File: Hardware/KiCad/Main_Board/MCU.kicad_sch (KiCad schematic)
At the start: 1 part, among them U2 Teensy4.1

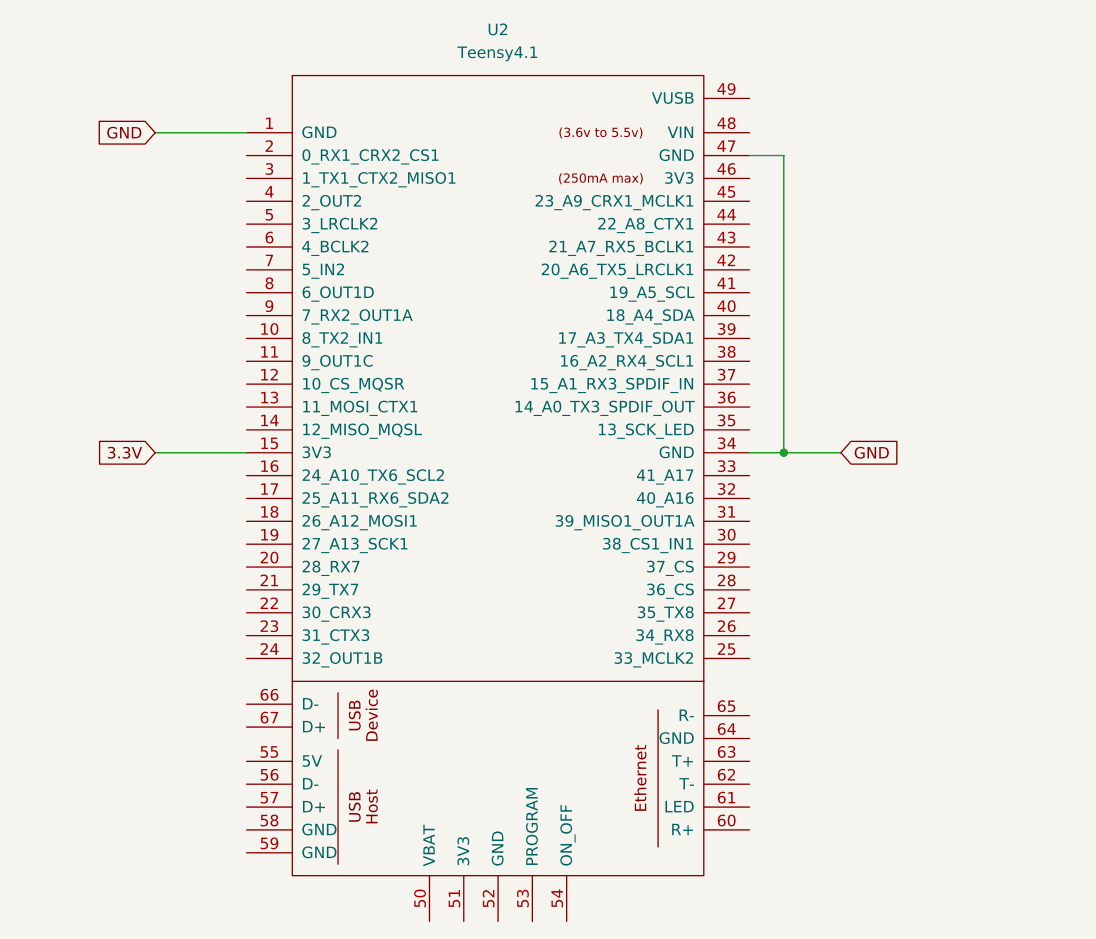
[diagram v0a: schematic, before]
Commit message: Created Female header connections for MCU
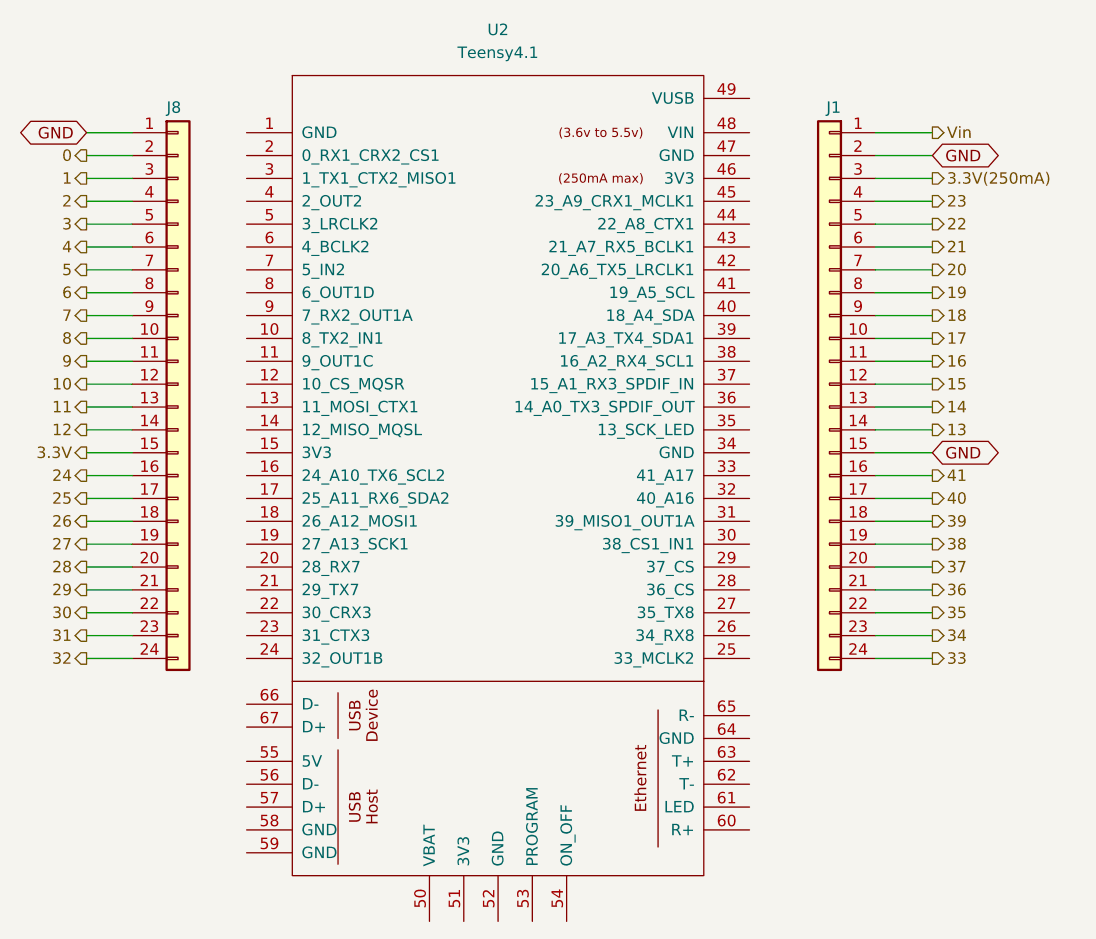
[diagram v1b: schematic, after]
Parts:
- added J1, J8: Conn_01x24_FPC, SparkFun-Connector:FPC_0.5mm-24-BottomContact, symbol SparkFun Connector:Conn_01x24_FPC_0.5mm-BottomContact
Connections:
- net 3.3V: now also J8.15 (Pin_15); no longer U2.15 (3V3)
- net GND: now also J1.15 (Pin_15), J1.2 (Pin_2), J8.1 (Pin_1); no longer U2.1 (GND), U2.34 (GND), U2.47 (GND)
- new net 0: J8.2 (Pin_2)
- new net 1: J8.3 (Pin_3)
- new net 10: J8.12 (Pin_12)
- new net 11: J8.13 (Pin_13)
- new net 12: J8.14 (Pin_14)
- new net 13: J1.14 (Pin_14)
- new net 14: J1.13 (Pin_13)
- new net 15: J1.12 (Pin_12)
- new net 16: J1.11 (Pin_11)
- new net 17: J1.10 (Pin_10)
- new net 18: J1.9 (Pin_9)
- new net 19: J1.8 (Pin_8)
- new net 2: J8.4 (Pin_4)
- new net 20: J1.7 (Pin_7)
- new net 21: J1.6 (Pin_6)
- new net 22: J1.5 (Pin_5)
- new net 23: J1.4 (Pin_4)
- new net 24: J8.16 (Pin_16)
- new net 25: J8.17 (Pin_17)
- new net 26: J8.18 (Pin_18)
- new net 27: J8.19 (Pin_19)
- new net 28: J8.20 (Pin_20)
- new net 29: J8.21 (Pin_21)
- new net 3: J8.5 (Pin_5)
- new net 3.3V(250mA): J1.3 (Pin_3)
- new net 30: J8.22 (Pin_22)
- new net 31: J8.23 (Pin_23)
- new net 32: J8.24 (Pin_24)
- new net 33: J1.24 (Pin_24)
- new net 34: J1.23 (Pin_23)
- new net 35: J1.22 (Pin_22)
- new net 36: J1.21 (Pin_21)
- new net 37: J1.20 (Pin_20)
- new net 38: J1.19 (Pin_19)
- new net 39: J1.18 (Pin_18)
- new net 4: J8.6 (Pin_6)
- new net 40: J1.17 (Pin_17)
- new net 41: J1.16 (Pin_16)
- new net 5: J8.7 (Pin_7)
- new net 6: J8.8 (Pin_8)
- new net 7: J8.9 (Pin_9)
- new net 8: J8.10 (Pin_10)
- new net 9: J8.11 (Pin_11)
- new net Vin: J1.1 (Pin_1)

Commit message: Experimental test points for USB data
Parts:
- added TP(D+), TP(D-): TestPoint, Sparkfun connector:TestPoint-1.25mm, symbol Connector:TestPoint
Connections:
- new net D+: TP(D+).1, TP(D-).1
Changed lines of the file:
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@@
+	(wire
+		(pts
+			(xy 106.68 143.51) (xy 109.22 143.51)
+		)
+		(stroke
+			(width 0)
+			(type default)
+		)
+	)
 	(wire
 		(pts
@@
 		(pts
 			(xy 194.31 92.71) (xy 200.66 92.71)
+		)
+		(stroke
+			(width 0)
+			(type default)
+		)
+	)
+	(wire
+		(pts
+			(xy 106.68 139.7) (xy 109.22 139.7)
 		)
 		(stroke
@@
 		)
 	)
+	(hierarchical_label "D+"
+		(shape input)
+		(at 106.68 139.7 180)
+		(effects
+			(font
+				(size 1.27 1.27)
+			)
+			(justify right)
+		)
+	)
 	(hierarchical_label "3.3V"
 		(shape output)
@@
 		(shape output)
 		(at 106.68 92.71 180)
+		(effects
+			(font
+				(size 1.27 1.27)
+			)
+			(justify right)
+		)
+	)
+	(hierarchical_label "D+"
+		(shape input)
+		(at 106.68 143.51 180)
 		(effects
 			(font
@@
 					(unit 1)
 				)
+			)
+		)
+	)
+	(symbol
+		(lib_id "Connector:TestPoint")
+		(at 109.22 143.51 270)
+		(unit 1)
+		(exclude_from_sim no)
+		(in_bom yes)
+		(on_board yes)
+		(dnp no)
+		(property "Reference" "TP(D-)"
+			(at 114.046 143.51 90)
+			(effects
+				(font
+					(size 1.27 1.27)
+				)
+				(justify left)
+			)
+		)
+		(property "Value" "TestPoint"
+			(at 111.2521 146.05 0)
+			(effects
+				(font
+					(size 1.27 1.27)
+				)
+				(justify left)
+				(hide yes)
+			)
+		)
+		(property "Footprint" "Sparkfun connector:TestPoint-1.25mm"
+			(at 109.22 148.59 0)
+			(effects
+				(font
+					(size 1.27 1.27)
+				)
+				(hide yes)
+			)
+		)
+		(property "Datasheet" "~"
+			(at 109.22 148.59 0)
+			(effects
+				(font
+					(size 1.27 1.27)
+				)
+				(hide yes)
+			)
+		)
+		(property "Description" "test point"
+			(at 109.22 143.51 0)
+			(effects
+				(font
+					(size 1.27 1.27)
+				)
+				(hide yes)
+			)
+		)
+		(pin "1"
+		)
+		(instances
+			(project "Main_Board"
+				(path "/e827c80a-ca8d-4d24-8db6-878b575a1aed/80744173-9491-4551-a74b-98f5922bdb3a"
+					(reference "TP(D-)")
+					(unit 1)
+				)
+			)
+		)
+	)
+	(symbol
+		(lib_id "Connector:TestPoint")
+		(at 109.22 139.7 270)
+		(unit 1)
+		(exclude_from_sim no)
+		(in_bom yes)
+		(on_board yes)
+		(dnp no)
+		(property "Reference" "TP(D+)"
+			(at 114.046 139.7 90)
+			(effects
+				(font
+					(size 1.27 1.27)
+				)
+				(justify left)
+			)
+		)
+		(property "Value" "TestPoint"
+			(at 111.2521 142.24 0)
+			(effects
+				(font
+					(size 1.27 1.27)
+				)
+				(justify left)
+				(hide yes)
+			)
+		)
+		(property "Footprint" "Sparkfun connector:TestPoint-1.25mm"
+			(at 109.22 144.78 0)
+			(effects
+				(font
+					(size 1.27 1.27)
+				)
+				(hide yes)
+			)
+		)
+		(property "Datasheet" "~"
+			(at 109.22 144.78 0)
+			(effects
+				(font
+					(size 1.27 1.27)
+				)
+				(hide yes)
+			)
+		)
+		(property "Description" "test point"
+			(at 109.22 139.7 0)
+			(effects
+				(font
+					(size 1.27 1.27)
+				)
+				(hide yes)
+			)
+		)
+		(pin "1"
+		)
+		(instances
+			(project ""
+				(path "/e827c80a-ca8d-4d24-8db6-878b575a1aed/80744173-9491-4551-a74b-98f5922bdb3a"
+					(reference "TP(D+)")
+					(unit 1)
+				)
